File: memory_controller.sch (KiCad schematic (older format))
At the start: 32 parts, among them U14 STM32F407VGTx

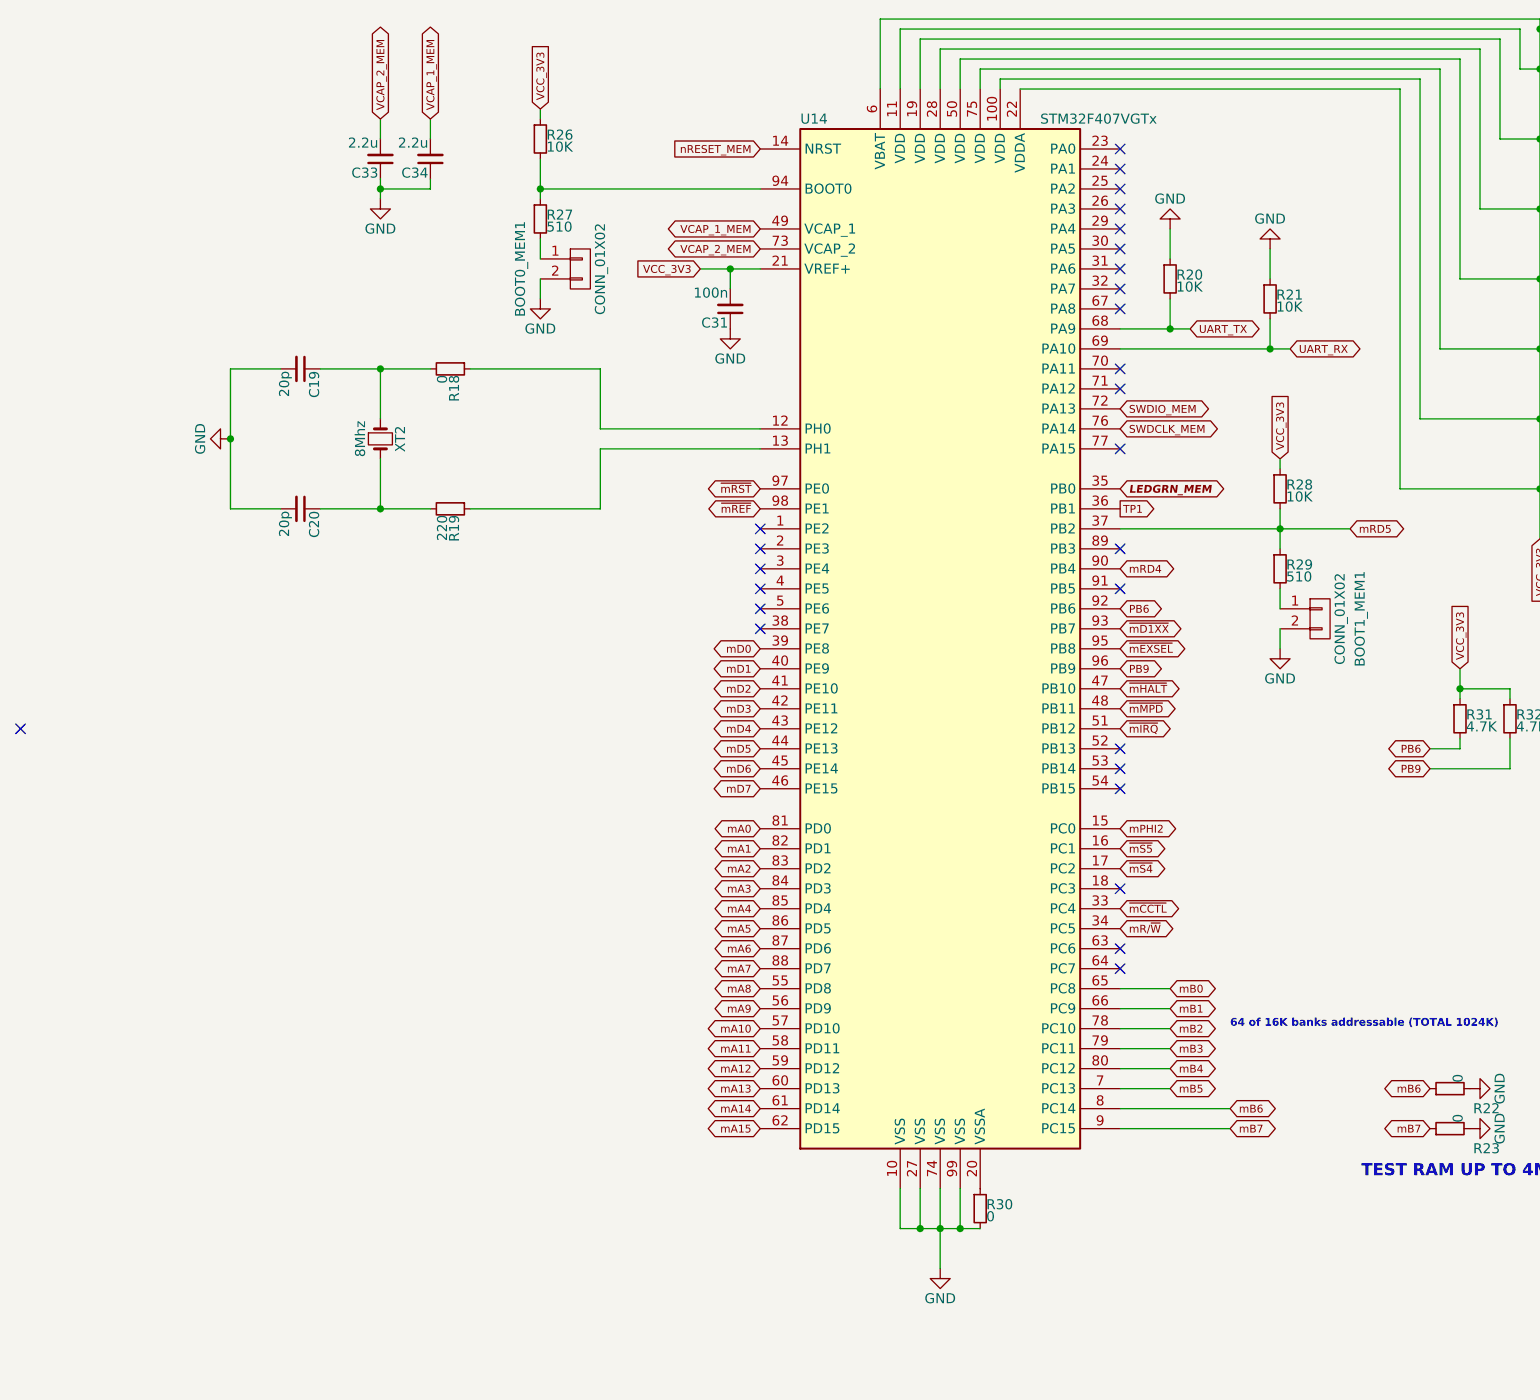
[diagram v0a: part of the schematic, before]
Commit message: Added a three channel dip-switch for select configuration
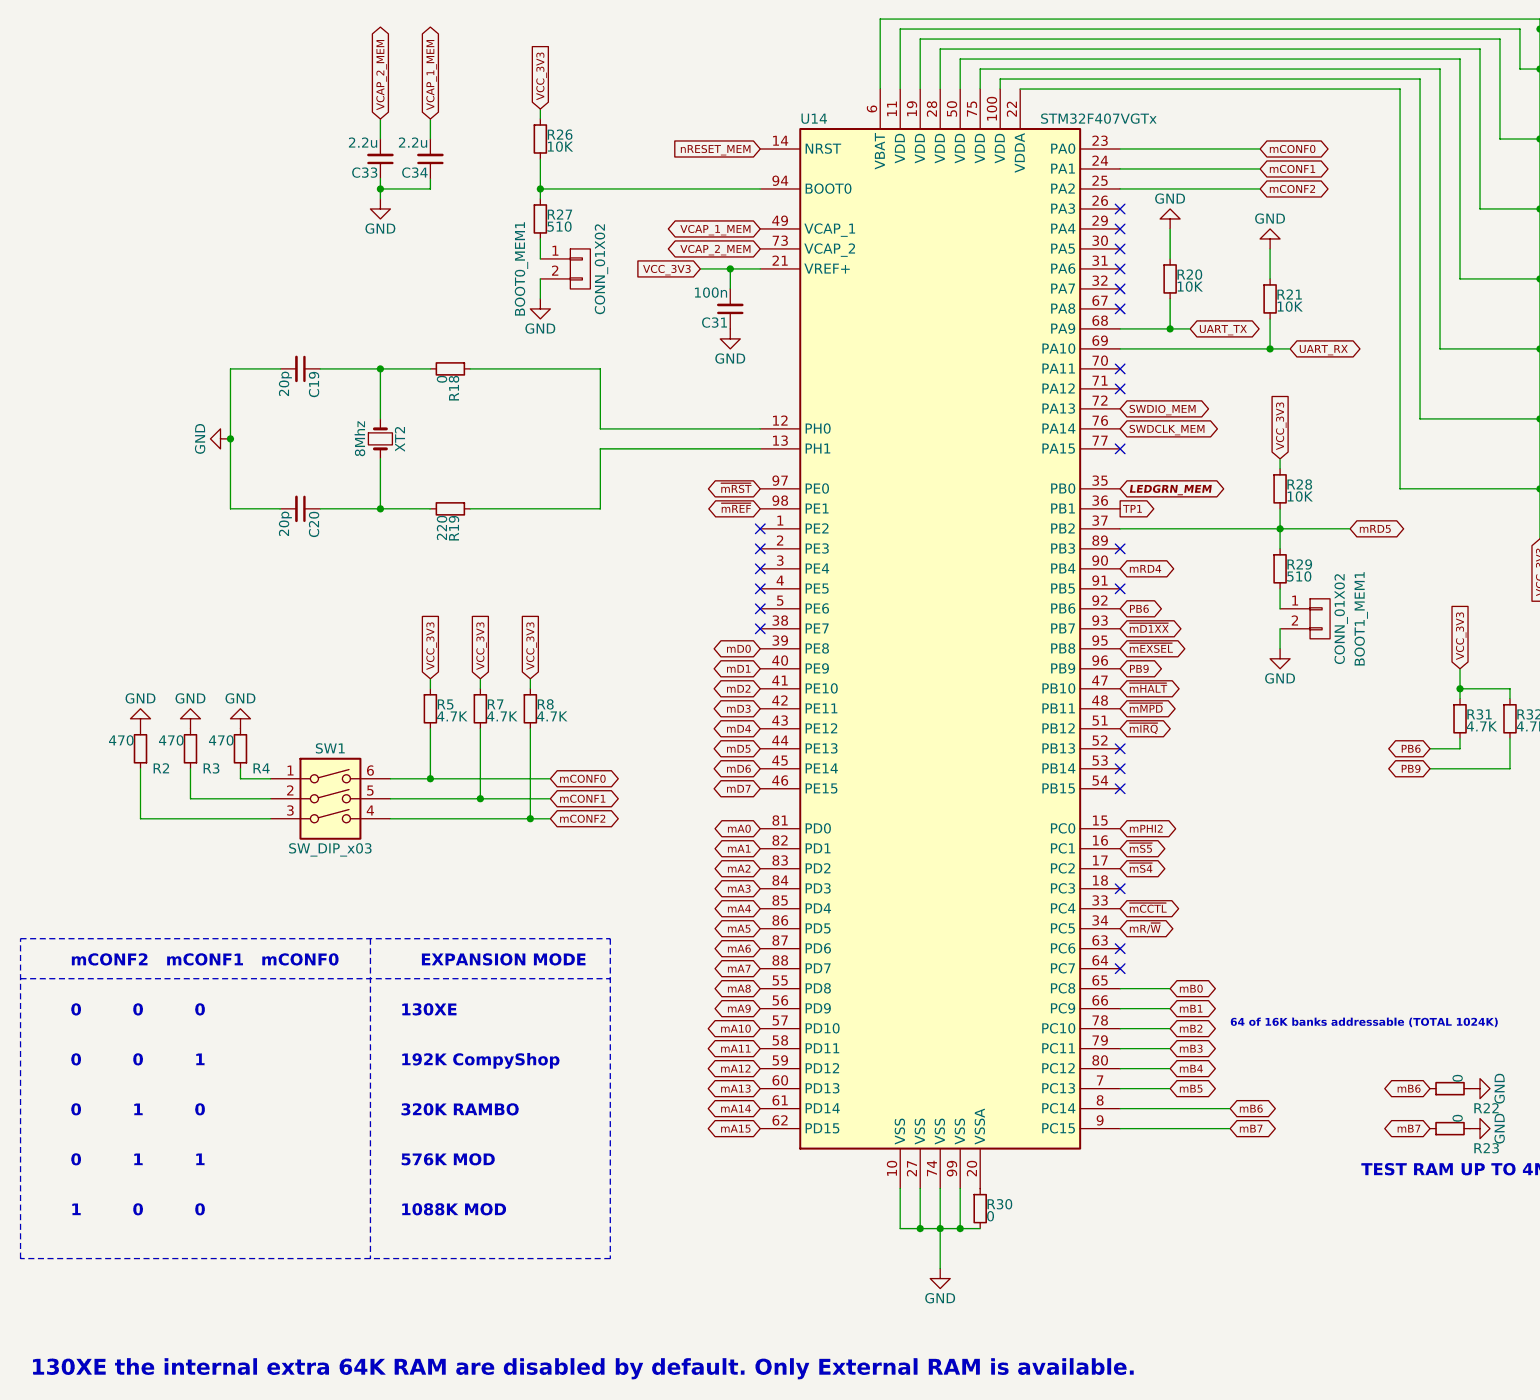
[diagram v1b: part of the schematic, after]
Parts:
- added R2, R3, R4: 470, Resistors_SMD:R_1206_HandSoldering, symbol R_Small
- added R5, R7, R8: 4.7K, Resistors_SMD:R_1206_HandSoldering, symbol R_Small
- added SW1: SW_DIP_x03, RetroBitLab:SW_DIP_SPSTx03_Slide_9.78x9.8mm_W8.61mm_P2.54mm, symbol SW_DIP_x03
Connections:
- net GND: now also R2.2, R3.2, R4.2
- net VCC_3V3: now also R5.1, R7.1, R8.1
- net mCONF0: now reaches U14.23 (PA0)
- net mCONF0: now also R5.2, SW1.6
- net mCONF1: now reaches U14.24 (PA1)
- net mCONF1: now also R7.2, SW1.5
- net mCONF2: now reaches U14.25 (PA2)
- net mCONF2: now also R8.2, SW1.4
- new net: R4.1, SW1.1
- new net: R3.1, SW1.2
- new net: R2.1, SW1.3
- no-connect marks 27 -> 23
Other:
- note added: "0 0 0"
- note added: "0 0 1"
- note added: "0 1 0"
- note added: "0 1 1"
- note added: "1 0 0"
- note added: "1088K MOD"
- note added: "130XE"
- note added: "130XE the internal extra 64K RAM are disabled by default. Only External RAM is available."
- note added: "192K CompyShop"
- note added: "320K RAMBO"
- note added: "576K MOD"
- note added: "EXPANSION MODE"
- note added: "mCONF2 mCONF1 mCONF0"
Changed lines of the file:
@@
 NoConn ~ 6200 1850
 NoConn ~ 6200 1750
-NoConn ~ 700  4150
 $Comp
 L R_Small R19
@@
 NoConn ~ 6200 1650
 NoConn ~ 6200 1550
-NoConn ~ 6200 1450
-NoConn ~ 6200 1350
-NoConn ~ 6200 1250
 NoConn ~ 6200 4950
 NoConn ~ 6200 5250
@@
 	6950 2250 6950 2100
 Wire Wire Line
-	6550 2150 6200 2150
+	6200 2150 6550 2150
 Wire Wire Line
 	6450 2000 6450 2150
@@
 NoConn ~ 6200 4350
 NoConn ~ 6200 4250
+$Comp
+L SW_DIP_x03 SW1
+U 1 1 5CF3CB14
+P 2250 4600
+F 0 "SW1" H 2250 4950 50  0000 C CNN
+F 1 "SW_DIP_x03" H 2250 4450 50  0000 C CNN
+F 2 "RetroBitLab:SW_DIP_SPSTx03_Slide_9.78x9.8mm_W8.61mm_P2.54mm" H 2250 4600 50  0001 C CNN
+F 3 "" H 2250 4600 50  0001 C CNN
+	1    2250 4600
+	1    0    0    -1
+$EndComp
+$Comp
+L R_Small R5
+U 1 1 5CF3CC0D
+P 2750 4050
+F 0 "R5" H 2780 4070 50  0000 L CNN
+F 1 "4.7K" H 2780 4010 50  0000 L CNN
+F 2 "Resistors_SMD:R_1206_HandSoldering" H 2750 4050 50  0001 C CNN
+F 3 "" H 2750 4050 50  0001 C CNN
+	1    2750 4050
+	1    0    0    -1
+$EndComp
+Wire Wire Line
+	2750 4150 2750 4400
+Text GLabel 2750 3900 1    39   Input ~ 0
+VCC_3V3
+Wire Wire Line
+	2750 3900 2750 3950
+$Comp
+L R_Small R7
+U 1 1 5CF3CEBD
+P 3000 4050
+F 0 "R7" H 3030 4070 50  0000 L CNN
+F 1 "4.7K" H 3030 4010 50  0000 L CNN
+F 2 "Resistors_SMD:R_1206_HandSoldering" H 3000 4050 50  0001 C CNN
+F 3 "" H 3000 4050 50  0001 C CNN
+	1    3000 4050
+	1    0    0    -1
+$EndComp
+Wire Wire Line
+	3000 4150 3000 4500
+Text GLabel 3000 3900 1    39   Input ~ 0
+VCC_3V3
+Wire Wire Line
+	3000 3900 3000 3950
+$Comp
+L R_Small R8
+U 1 1 5CF3CF1F
+P 3250 4050
+F 0 "R8" H 3280 4070 50  0000 L CNN
+F 1 "4.7K" H 3280 4010 50  0000 L CNN
+F 2 "Resistors_SMD:R_1206_HandSoldering" H 3250 4050 50  0001 C CNN
+F 3 "" H 3250 4050 50  0001 C CNN
+	1    3250 4050
+	1    0    0    -1
+$EndComp
+Wire Wire Line
+	3250 4150 3250 4600
+Text GLabel 3250 3900 1    39   Input ~ 0
+VCC_3V3
+Wire Wire Line
+	3250 3900 3250 3950
+Wire Wire Line
+	2550 4400 3350 4400
+Wire Wire Line
+	2550 4500 3350 4500
+Wire Wire Line
+	2550 4600 3350 4600
+Connection ~ 3250 4600
+Connection ~ 3000 4500
+Connection ~ 2750 4400
+$Comp
+L R_Small R4
+U 1 1 5CF3D4D2
+P 1800 4250
+F 0 "R4" H 1650 4350 50  0000 L CNN
+F 1 "470" H 1830 4210 50  0000 L CNN
+F 2 "Resistors_SMD:R_1206_HandSoldering" H 1800 4250 50  0001 C CNN
+F 3 "" H 1800 4250 50  0001 C CNN
+	1    1800 4250
+	-1   0    0    1
+$EndComp
+$Comp
+L GND #PWR032
+U 1 1 5CF3D4D8
+P 1800 4150
+F 0 "#PWR032" H 1800 3900 50  0001 C CNN
+F 1 "GND" H 1800 4000 50  0000 C CNN
+F 2 "" H 1800 4150 50  0001 C CNN
+F 3 "" H 1800 4150 50  0001 C CNN
+	1    1800 4150
+	-1   0    0    1
+$EndComp
+$Comp
+L R_Small R3
+U 1 1 5CF3D842
+P 1550 4250
+F 0 "R3" H 1400 4350 50  0000 L CNN
+F 1 "470" H 1580 4210 50  0000 L CNN
+F 2 "Resistors_SMD:R_1206_HandSoldering" H 1550 4250 50  0001 C CNN
+F 3 "" H 1550 4250 50  0001 C CNN
+	1    1550 4250
+	-1   0    0    1
+$EndComp
+$Comp
+L GND #PWR033
+U 1 1 5CF3D8CC
+P 1550 4150
+F 0 "#PWR033" H 1550 3900 50  0001 C CNN
+F 1 "GND" H 1550 4000 50  0000 C CNN
+F 2 "" H 1550 4150 50  0001 C CNN
+F 3 "" H 1550 4150 50  0001 C CNN
+	1    1550 4150
+	-1   0    0    1
+$EndComp
+$Comp
+L R_Small R2
+U 1 1 5CF3D949
+P 1300 4250
+F 0 "R2" H 1150 4350 50  0000 L CNN
+F 1 "470" H 1330 4210 50  0000 L CNN
+F 2 "Resistors_SMD:R_1206_HandSoldering" H 1300 4250 50  0001 C CNN
+F 3 "" H 1300 4250 50  0001 C CNN
+	1    1300 4250
+	-1   0    0    1
+$EndComp
+$Comp
+L GND #PWR034
+U 1 1 5CF3D9DA
+P 1300 4150
+F 0 "#PWR034" H 1300 3900 50  0001 C CNN
+F 1 "GND" H 1300 4000 50  0000 C CNN
+F 2 "" H 1300 4150 50  0001 C CNN
+F 3 "" H 1300 4150 50  0001 C CNN
+	1    1300 4150
+	-1   0    0    1
+$EndComp
+Wire Wire Line
+	1800 4350 1800 4400
+Wire Wire Line
+	1800 4400 1950 4400
+Wire Wire Line
+	1950 4500 1550 4500
+Wire Wire Line
+	1550 4500 1550 4350
+Wire Wire Line
+	1950 4600 1300 4600
+Wire Wire Line
+	1300 4600 1300 4350
+Text GLabel 3350 4400 2    39   BiDi ~ 0
+mCONF0
+Text GLabel 3350 4500 2    39   BiDi ~ 0
+mCONF1
+Text GLabel 3350 4600 2    39   BiDi ~ 0
+mCONF2
+Text GLabel 6900 1250 2    39   BiDi ~ 0
+mCONF0
+Text GLabel 6900 1350 2    39   BiDi ~ 0
+mCONF1
+Text GLabel 6900 1450 2    39   BiDi ~ 0
+mCONF2
+Wire Wire Line
+	6200 1250 6900 1250
+Wire Wire Line
+	6900 1350 6200 1350
+Wire Wire Line
+	6200 1450 6900 1450
+Text Notes 950  5350 0    59   ~ 12
+mCONF2   mCONF1   mCONF0
+Text Notes 950  5600 0    59   ~ 12
+      0         0         0
+Text Notes 950  5850 0    59   ~ 12
+      0         0         1
+Text Notes 950  6100 0    59   ~ 12
+      0         1         0
+Text Notes 950  6350 0    59   ~ 12
+      0         1         1
+Text Notes 950  6600 0    59   ~ 12
+      1         0         0
+Text Notes 2600 5600 0    59   ~ 12
+130XE
+Text Notes 2600 5850 0    59   ~ 12
+192K CompyShop
+Text Notes 2600 6100 0    59   ~ 12
+320K RAMBO
+Text Notes 2600 6350 0    59   ~ 12
+576K MOD
+Text Notes 2600 6600 0    59   ~ 12
+1088K MOD
+Wire Notes Line
+	700  5200 3650 5200
+Wire Notes Line
+	3650 5200 3650 6800
+Wire Notes Line
+	3650 6800 700  6800
+Wire Notes Line
+	700  6800 700  5200
+Wire Notes Line
+	700  5400 3650 5400
+Wire Notes Line
+	2450 5200 2450 6800
+Text Notes 2700 5350 0    59   ~ 12
+EXPANSION MODE
+Text Notes 750  7400 0    79   ~ 16
+130XE the internal extra 64K RAM are disabled by default. Only External RAM is available.
 $EndSCHEMATC
